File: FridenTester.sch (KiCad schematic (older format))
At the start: 22 parts, among them P1 CONN_02X05, U1 BSD223P, U10 BSD223P, U11 BSD223P, U12 2N7002DN, U13 2N7002DN, U14 BSD223P, U15 BSD223P, U16 2N7002DN, U17 2N7002DN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

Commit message: Added text, images
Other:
- note added: "5V/12V UNIDIRECTIONAL LEVEL SHIFTER"
- note added: "This work is licensed under the Creative Commons Attribution-ShareAlike 4.0 \nInternational License. To view a copy of this license, visit\nhttp://creativecommons.org/licenses/by-sa/4.0/ or send a letter to \nCreative Commons, PO Box 1866, Mountain View, CA 94042, USA.\n\nAttribution: Robert Baruch (robert.c.baruch@gmail.com)"
- note added: "VDD is logic-level voltage: 5v or 3v3.\n\nSW_A and SW_B are logic-level inputs. For 0, translation is from \nIO12 to IO5. For 1, translation is from IO5 to IO12."

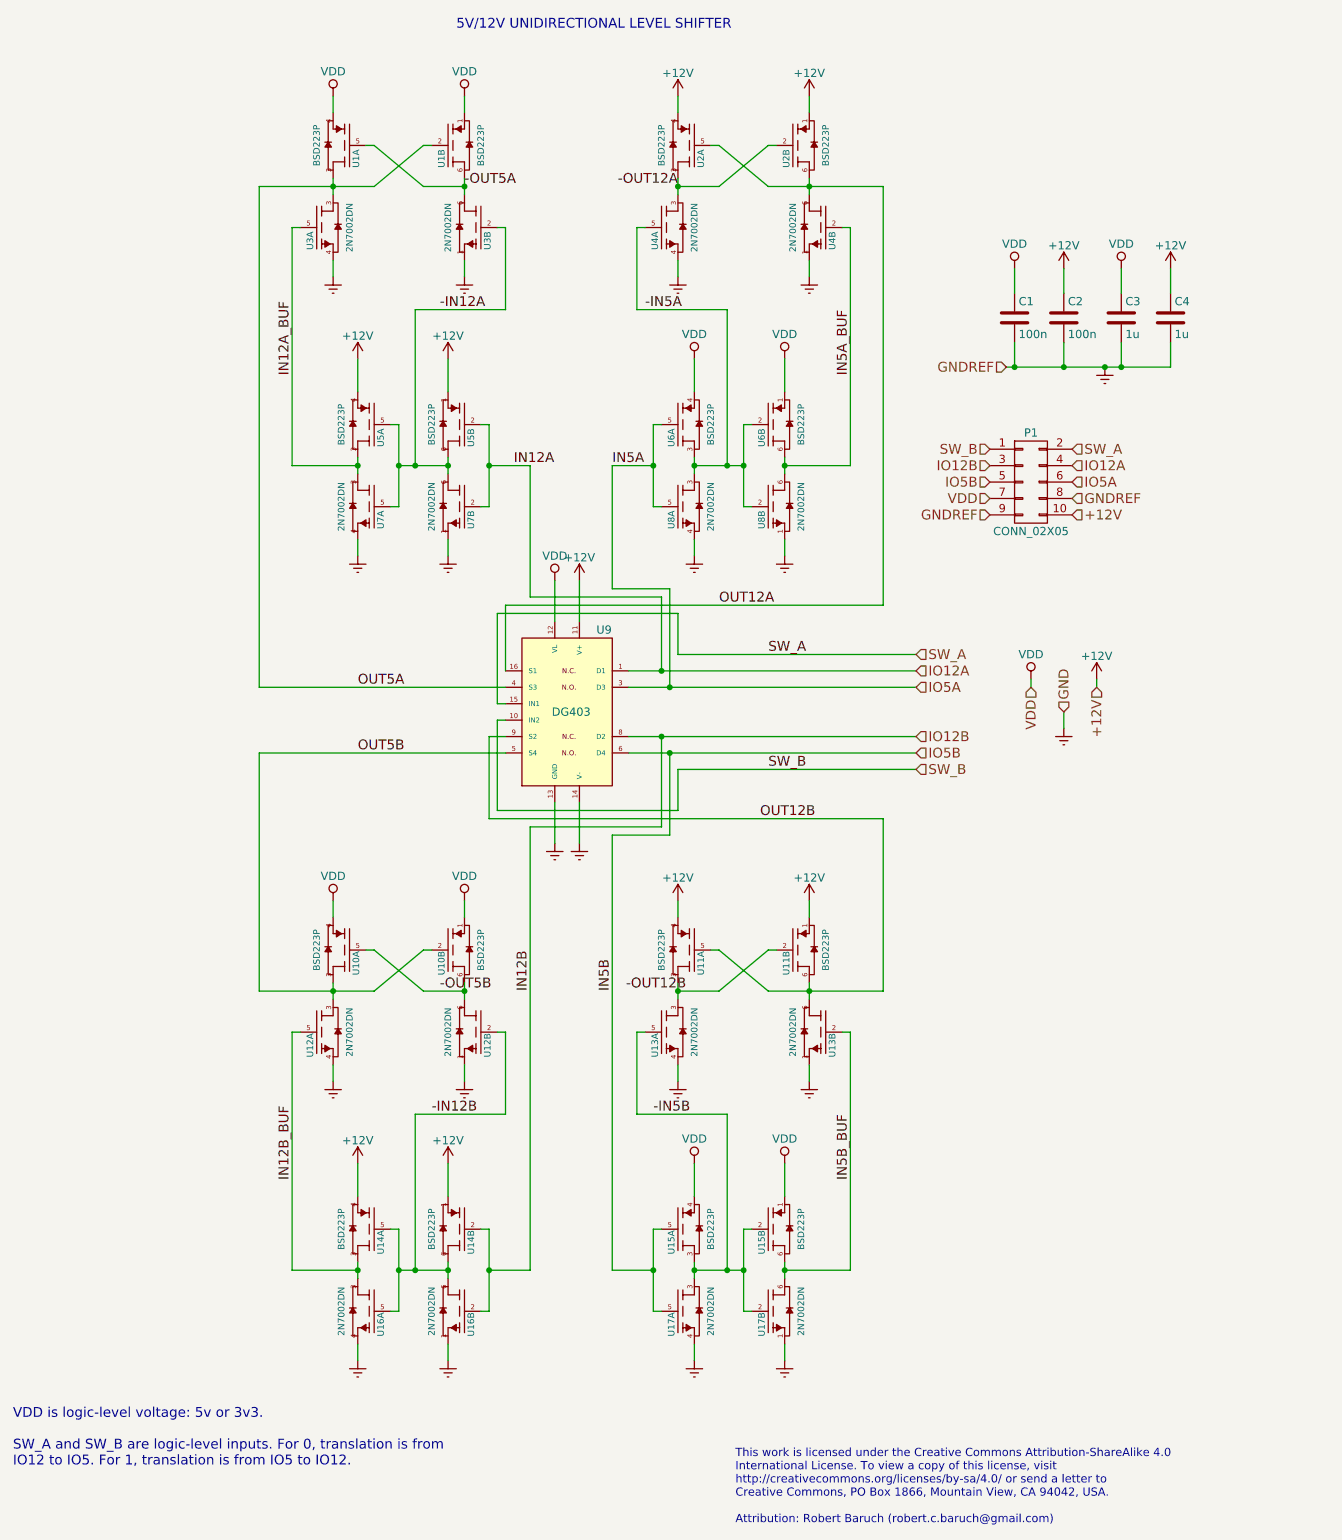
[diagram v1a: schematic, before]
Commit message: Revision C, with gate drivers instead of mosfets
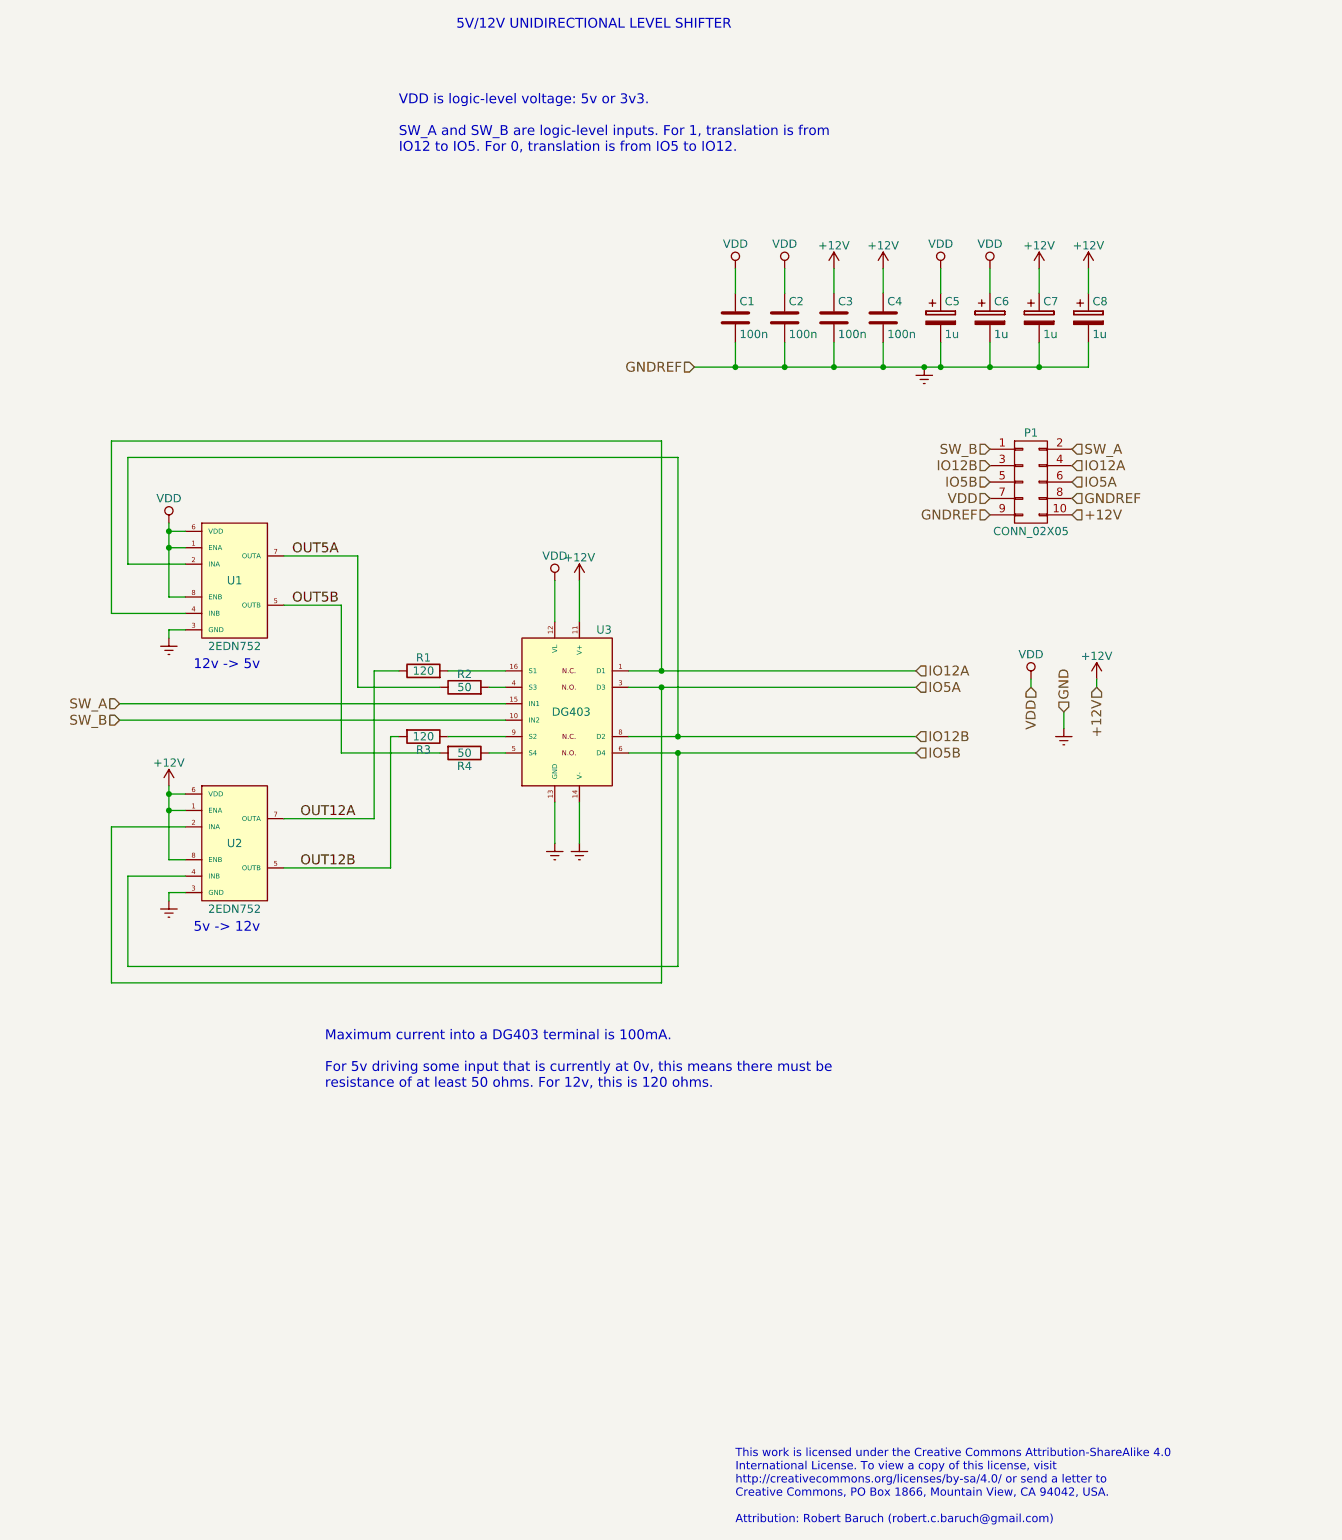
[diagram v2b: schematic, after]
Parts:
- removed C3: 1u, Capacitors_SMD:C_1206, symbol C
- removed U1, U10, U11, U14, U15, U2, U5, U6: BSD223P, friden-footprints:SOT-363, symbol BSD223P
- removed U12, U13, U16, U17, U3, U4, U7, U8: 2N7002DN, friden-footprints:SOT-363, symbol 2N7002DN
- added C1: 100n, Capacitors_SMD:C_1206, symbol C
- added C5, C6, C7, C8: 1u, Capacitors_SMD:C_1206, symbol CP
- added R1, R3: 120, Resistors_SMD:R_1206, symbol R
- added R2, R4: 50, Resistors_SMD:R_1206, symbol R
- added U1, U2: 2EDN752, Housings_SOIC:SOIC-8_3.9x4.9mm_Pitch1.27mm, symbol 2EDN752
- C4: value 1u -> 100n
- renumbered C1 to C2, C2 to C3, U9 to U3
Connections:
- net +12V: now also C7.1, C8.1, U2.1 (ENA), U2.6 (VDD), U2.8 (ENB)
- net GNDREF: now also C1.2, C5.2, C6.2, C7.2, C8.2, U1.3 (GND), U2.3 (GND)
- net IO12A: now also U1.4 (INB)
- net IO12B: now also U1.2 (INA)
- net IO5A: now also U2.2 (INA)
- net IO5B: now also U2.4 (INB)
- net OUT12A: now also R1.1, U2.7 (OUTA); no longer U3.16 (S1)
- net OUT12B: now also R3.2, U2.5 (OUTB); no longer U3.9 (S2)
- net OUT5A: now also R2.1, U1.7 (OUTA); no longer U3.4 (S3)
- net OUT5B: now also R4.2, U1.5 (OUTB); no longer U3.5 (S4)
- net VDD: now also C1.1, C5.1, C6.1, U1.1 (ENA), U1.6 (VDD), U1.8 (ENB)
- new net: R1.2, U3.16 (S1)
- new net: R2.2, U3.4 (S3)
- new net: R4.1, U3.5 (S4)
- new net: R3.1, U3.9 (S2)
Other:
- note added: "12v -> 5v"
- note added: "5v -> 12v"
- note added: "Maximum current into a DG403 terminal is 100mA.\n\nFor 5v driving some input that is currently at 0v, this means there must be\nresistance of at least 50 ohms. For 12v, this is 120 ohms."
- note added: "VDD is logic-level voltage: 5v or 3v3.\n\nSW_A and SW_B are logic-level inputs. For 1, translation is from \nIO12 to IO5. For 0, translation is from IO5 to IO12."
- note removed: "VDD is logic-level voltage: 5v or 3v3.\n\nSW_A and SW_B are logic-level inputs. For 0, translation is from \nIO12 to IO5. For 1, translation is from IO5 to IO12."
- moved on the sheet: C2, C3
